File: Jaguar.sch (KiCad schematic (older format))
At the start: 29 parts, among them J2 TE-34, P1 12v-SW, P10 TPS, P11 TPS-GND, P12 O2, P13 O2-GND, P14 CRANK+, P15 CRANK-, P16 CAM+, P17 CAM-, P18 DIS-BYPASS, P19 IGN-ADVANCE, P2 12v-SW2, P20 PT3-5, P21 Inj-IN, P22 INJ-GND, P25 FUEL-, P26 Injectors, P3 GND, P31 OUT-GND, P32 OUT-12v, P33 Injectors-PB, P34 Injectors, P4 BRV-12v, P5 GND2, P6 IAT, P7 MAT, P8 COOLANT, P9 TPS-5v

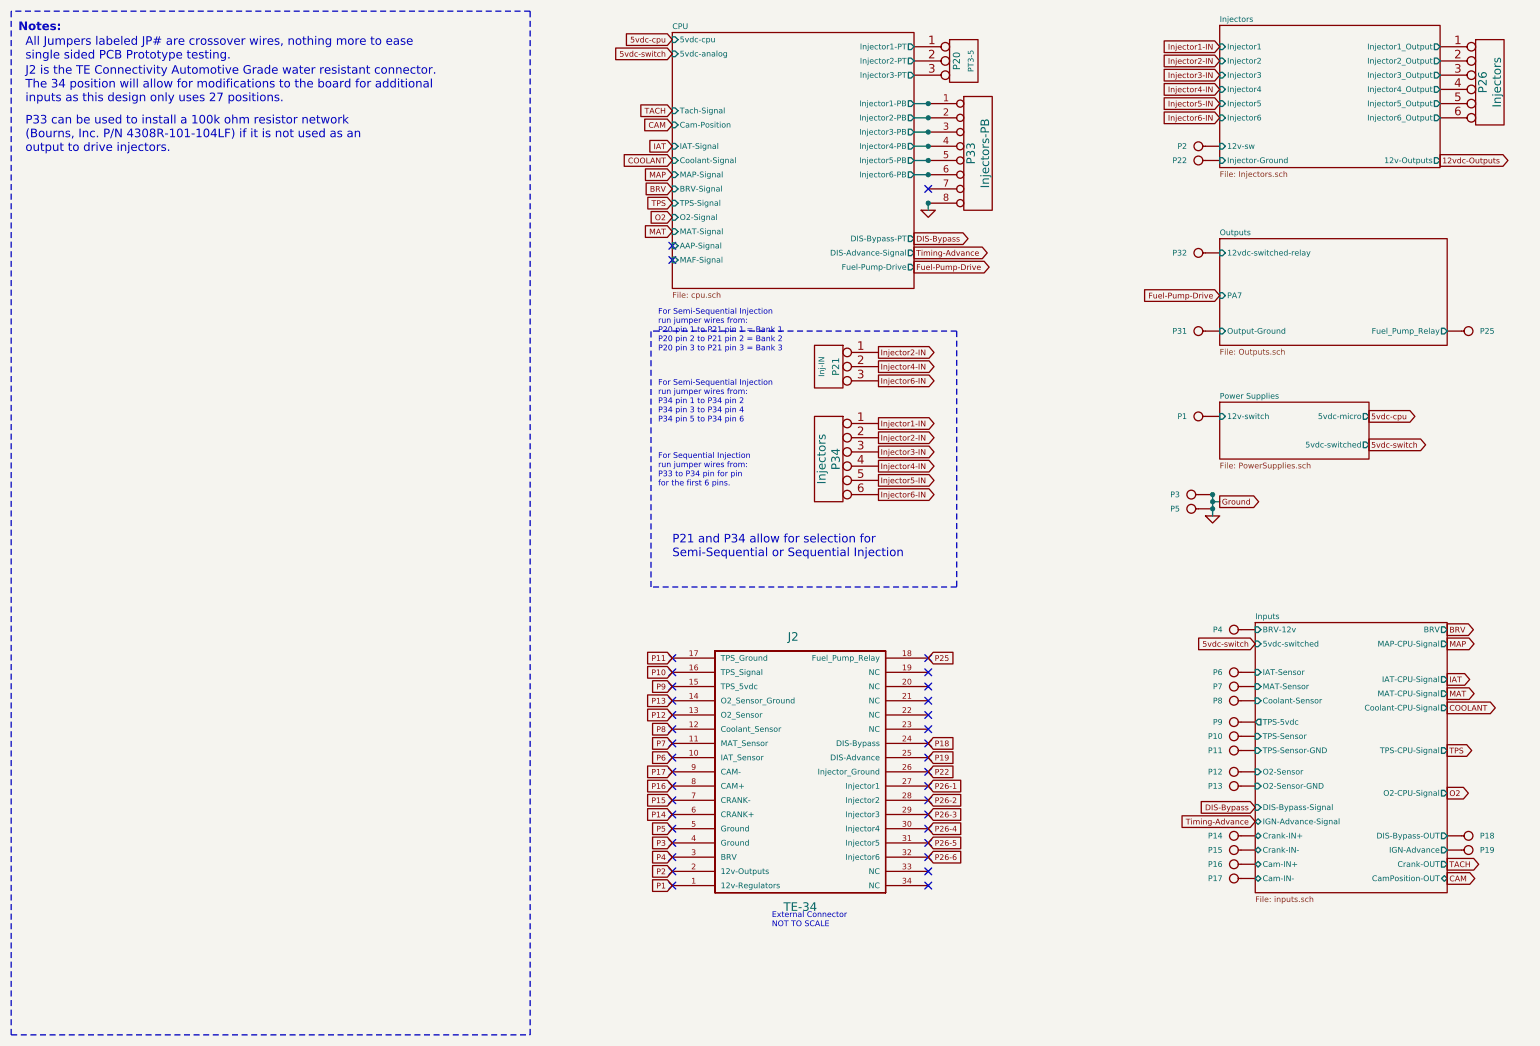
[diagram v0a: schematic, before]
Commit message: Updated Schematics, PDF, BOM for 4cyl Sequential Injection
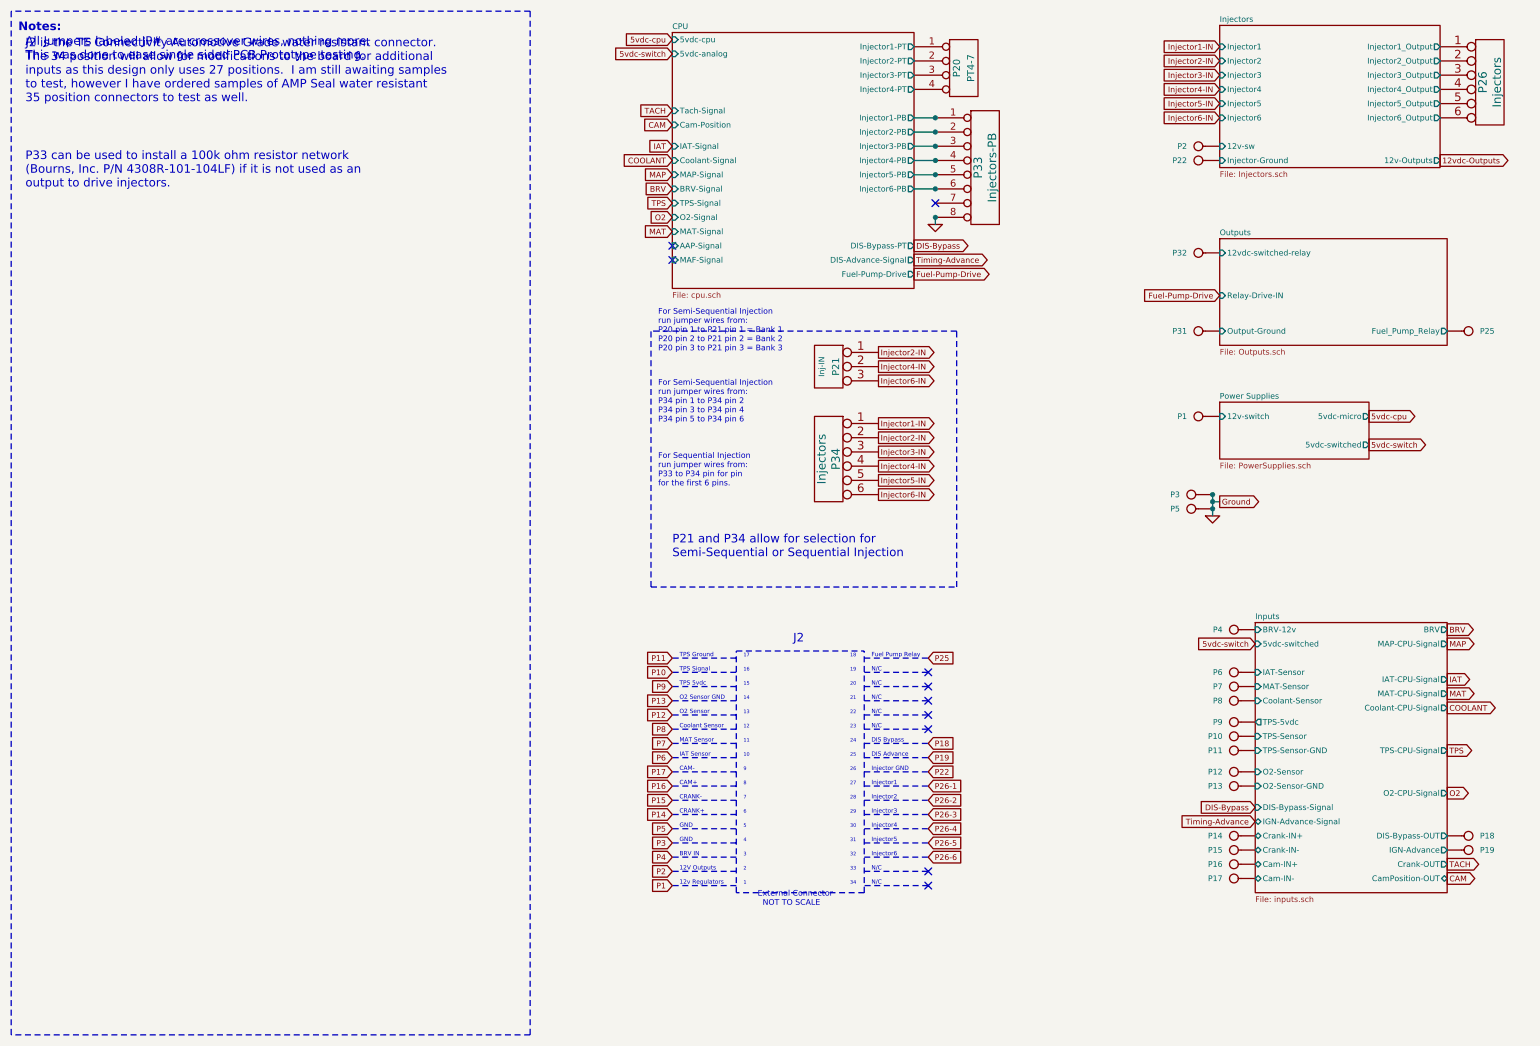
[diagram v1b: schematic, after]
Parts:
- removed J2: TE-34, symbol TE-34
- removed P20: PT3-5, symbol CONN_3
- added P20: PT4-7, symbol CONN_4
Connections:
- net CPU/Injector1-PT: now also P20.1 (P1)
- net CPU/Injector2-PT: now also P20.2 (P2)
- net CPU/Injector3-PT: now also P20.3 (P3)
- new net CPU/Injector4-PT: P20.4 (P4)
- no-connect marks 37 -> 10
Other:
- note added: "1"
- note added: "10"
- note added: "11"
- note added: "12"
- note added: "12V Outputs"
- note added: "12v Regulators"
- note added: "13"
- note added: "14"
- note added: "15"
- note added: "16"
- note added: "17"
- note added: "18"
- note added: "19"
- note added: "2"
- note added: "20"
- note added: "21"
- note added: "22"
- note added: "23"
- note added: "24"
- note added: "25"
- note added: "26"
- note added: "27"
- note added: "28"
- note added: "29"
- note added: "3"
- note added: "30"
- note added: "31"
- note added: "32"
- note added: "33"
- note added: "34"
- note added: "4"
- note added: "5"
- note added: "6"
- note added: "7"
- note added: "8"
- note added: "9"
- note added: "All Jumpers labeled JP# are crossover wires, nothing more.\nThis was done to ease single sided PCB Prototype testing."
- note added: "BRV IN"
- note added: "CAM+"
- note added: "CAM-"
- note added: "CRANK+"
- note added: "CRANK-"
- note added: "Coolant Sensor"
- note added: "DIS Advance"
- note added: "DIS Bypass"
- note added: "External Connector\n NOT TO SCALE"
- note added: "Fuel Pump Relay"
- note added: "GND"
- note added: "IAT Sensor"
- note added: "Injector GND"
- note added: "Injector1"
- note added: "Injector2"
- note added: "Injector3"
- note added: "Injector4"
- note added: "Injector5"
- note added: "Injector6"
- note added: "J2"
- note added: "J2 is the TE Connectivity Automotive Grade water resistant connector. \nThe 34 position will allow for modifications to the board for additional \ninputs as this design only uses 27 positions. I am still awaiting samples\nto test, however I have ordered samples of AMP Seal water resistant\n35 position connectors to test as well."
- note added: "MAT Sensor"
- note added: "N/C"
- note added: "O2 Sensor"
- note added: "O2 Sensor GND"
- note added: "TPS 5vdc"
- note added: "TPS Ground"
- note added: "TPS Signal"
- note removed: "All Jumpers labeled JP# are crossover wires, nothing more to ease \nsingle sided PCB Prototype testing."
- note removed: "External Connector\nNOT TO SCALE"
- note removed: "J2 is the TE Connectivity Automotive Grade water resistant connector. \nThe 34 position will allow for modifications to the board for additional \ninputs as this design only uses 27 positions."
- moved on the sheet: P33

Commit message: Updated everything for up to 8 cylinder engines
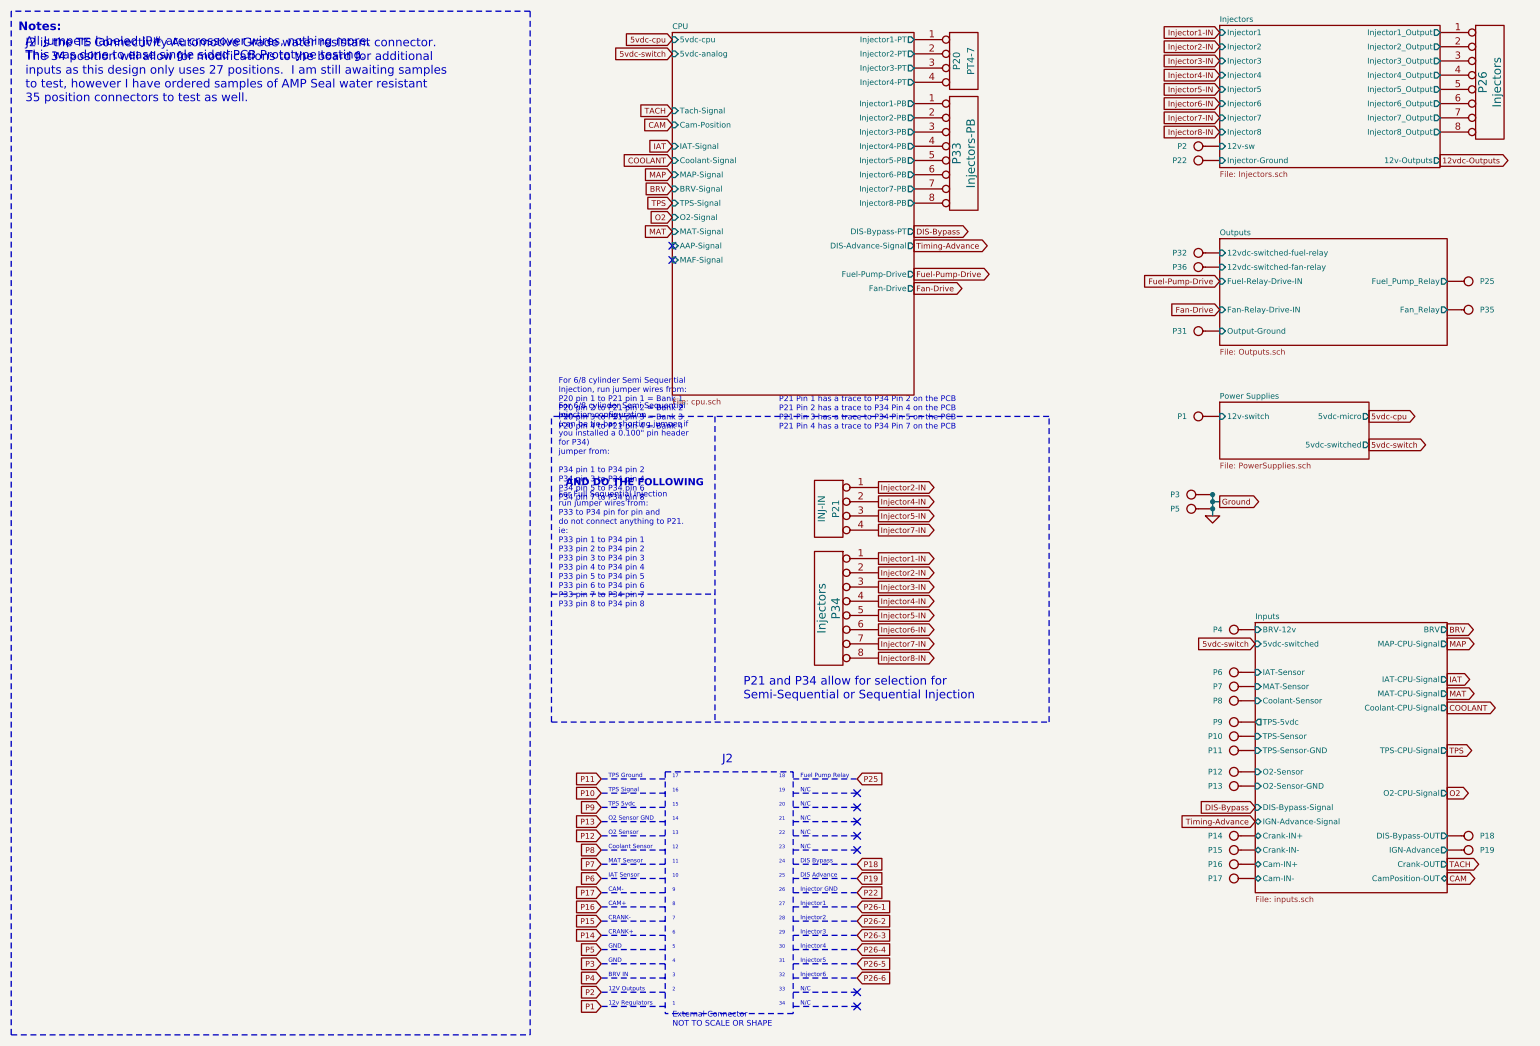
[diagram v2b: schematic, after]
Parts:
- removed P21: Inj-IN, symbol CONN_3
- removed P26, P34: Injectors, symbol CONN_6
- added P21: INJ-IN, symbol CONN_4
- added P26, P34: Injectors, symbol CONN_8
- added P35: FAN-, symbol CONN_1
- added P36: FAN-12v, symbol CONN_1
- P32: value OUT-12v -> FUEL-12v
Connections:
- net GND: no longer P33.8 (P8)
- net Injector1-IN: now also P34.1 (P1)
- net Injector2-IN: now also P21.1 (P1), P34.2 (P2)
- net Injector3-IN: now also P34.3 (P3)
- net Injector4-IN: now also P21.2 (P2), P34.4 (P4)
- net Injector5-IN: now also P21.3 (P3), P34.5 (P5)
- net Injector6-IN: now also P34.6 (P6)
- net Injectors/Injector1_Output: now also P26.1 (P1)
- net Injectors/Injector2_Output: now also P26.2 (P2)
- net Injectors/Injector3_Output: now also P26.3 (P3)
- net Injectors/Injector4_Output: now also P26.4 (P4)
- net Injectors/Injector5_Output: now also P26.5 (P5)
- net Injectors/Injector6_Output: now also P26.6 (P6)
- net CPU/Injector7-PB: now reaches P33.7 (P7)
- net Outputs/12vdc-switched-relay renamed Outputs/12vdc-switched-fuel-relay
- new net CPU/Injector8-PB: P33.8 (P8)
- new net Injector7-IN: P21.4 (P4), P34.7 (P7)
- new net Injector8-IN: P34.8 (P8)
- new net Injectors/Injector7_Output: P26.7 (P7)
- new net Injectors/Injector8_Output: P26.8 (P8)
- new net Outputs/12vdc-switched-fan-relay: P36.1
- new net Outputs/Fan_Relay: P35.1
- no-connect marks 10 -> 9
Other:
- note added: "AND DO THE FOLLOWING"
- note added: "External Connector\nNOT TO SCALE OR SHAPE"
- note added: "For 6/8 cylinder Semi Sequential\nInjection configuration\n(can be tie-bar shorting jumper if \nyou installed a 0.100" pin header \nfor P34)\njumper from:\n\nP34 pin 1 to P34 pin 2\nP34 pin 3 to P34 pin 4\nP34 pin 5 to P34 pin 6\nP34 pin 7 to P34 pin 8"
- note added: "For 6/8 cylinder Semi Sequential\nInjection, run jumper wires from: \nP20 pin 1 to P21 pin 1 = Bank 1\nP20 pin 2 to P21 pin 2 = Bank 2\nP20 pin 3 to P21 pin 3 = Bank 3\nP20 pin 4 to P21 pin 4 = Bank 4"
- note added: "For Full Sequential Injection\nrun jumper wires from:\nP33 to P34 pin for pin and \ndo not connect anything to P21.\nie: \nP33 pin 1 to P34 pin 1\nP33 pin 2 to P34 pin 2\nP33 pin 3 to P34 pin 3\nP33 pin 4 to P34 pin 4\nP33 pin 5 to P34 pin 5\nP33 pin 6 to P34 pin 6\nP33 pin 7 to P34 pin 7\nP33 pin 8 to P34 pin 8\n"
- note added: "P21 Pin 1 has a trace to P34 Pin 2 on the PCB\nP21 Pin 2 has a trace to P34 Pin 4 on the PCB\nP21 Pin 3 has a trace to P34 Pin 5 on the PCB\nP21 Pin 4 has a trace to P34 Pin 7 on the PCB"
- note removed: "External Connector\n NOT TO SCALE"
- note removed: "For Semi-Sequential Injection \nrun jumper wires from: \nP20 pin 1 to P21 pin 1 = Bank 1\nP20 pin 2 to P21 pin 2 = Bank 2\nP20 pin 3 to P21 pin 3 = Bank 3"
- note removed: "For Semi-Sequential Injection\nrun jumper wires from:\nP34 pin 1 to P34 pin 2\nP34 pin 3 to P34 pin 4\nP34 pin 5 to P34 pin 6"
- note removed: "For Sequential Injection\nrun jumper wires from:\nP33 to P34 pin for pin\nfor the first 6 pins.\n"
- note removed: "P33 can be used to install a 100k ohm resistor network \n(Bourns, Inc. P/N 4308R-101-104LF) if it is not used as an\noutput to drive injectors."
- moved on the sheet: P20, P25, P33
